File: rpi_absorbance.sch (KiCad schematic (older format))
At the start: 33 parts, among them CON1 BARREL_JACK, P1 CONN_02X04, P2 CONN_01X02, P3 RPI_HEADER, P4 STEPPER_CONN, P5 CONN_02X05, Q1 ZTX692B, U1 R-78B5.0-1.5L, U2 MUN5216DW1T1G, U3 DRV8825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

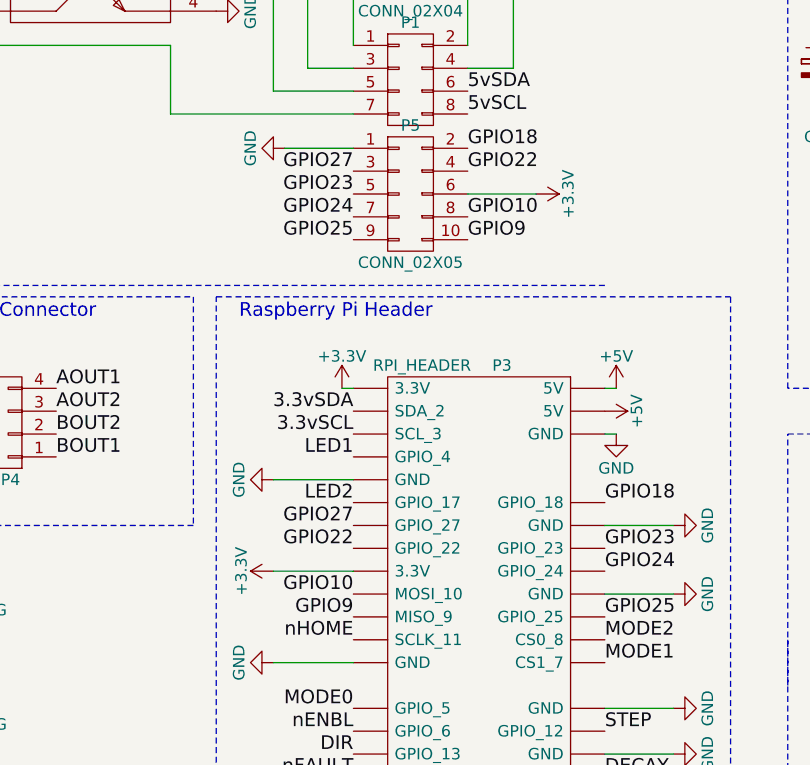
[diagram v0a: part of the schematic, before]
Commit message: Add missing connections
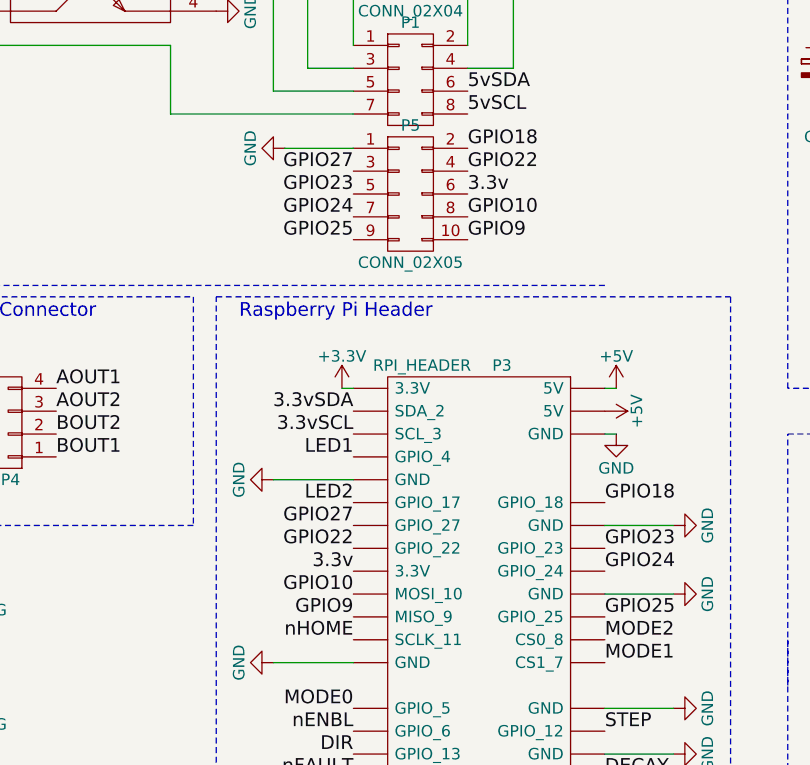
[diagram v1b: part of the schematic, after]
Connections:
- net +3V3: no longer P3.17 (3.3V), P5.6 (P6)
- new net 3.3v: P3.17 (3.3V), P5.6 (P6)
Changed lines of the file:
@@
 LED1
-$Comp
-L +3.3V #PWR021
-U 1 1 56CC6368
-P 2750 6050
-F 0 "#PWR021" H 2750 5900 50  0001 C CNN
-F 1 "+3.3V" H 2750 6190 50  0000 C CNN
-F 2 "" H 2750 6050 50  0000 C CNN
-F 3 "" H 2750 6050 50  0000 C CNN
-	1    2750 6050
-	0    -1   -1   0
-$EndComp
 $Comp
 L PWR_FLAG #FLG022
@@
 Text Notes 5100 2800 0    60   ~ 0
 Stepper Motor Driver
-$Comp
-L +3.3V #PWR040
-U 1 1 56CD7200
-P 3900 4400
-F 0 "#PWR040" H 3900 4250 50  0001 C CNN
-F 1 "+3.3V" H 3900 4540 50  0000 C CNN
-F 2 "" H 3900 4400 50  0000 C CNN
-F 3 "" H 3900 4400 50  0000 C CNN
-	1    3900 4400
-	0    1    1    0
-$EndComp
 $Comp
 L RPI_HEADER P3
@@
 Wire Notes Line
 	5000 5250 5000 2700
-Wire Wire Line
-	2750 6050 3100 6050
 Wire Notes Line
 	2500 4850 4750 4850
@@
 Text Label 3100 4600 2    60   ~ 0
 GPIO25
-Wire Wire Line
-	3900 4400 3600 4400
 Text Label 3100 4300 2    60   ~ 0
 GPIO27
@@
 $EndComp
 Connection ~ 2300 2500
+Text Label 3100 6050 2    60   ~ 0
+3.3v
+Text Label 3600 4400 0    60   ~ 0
+3.3v
 $EndSCHEMATC

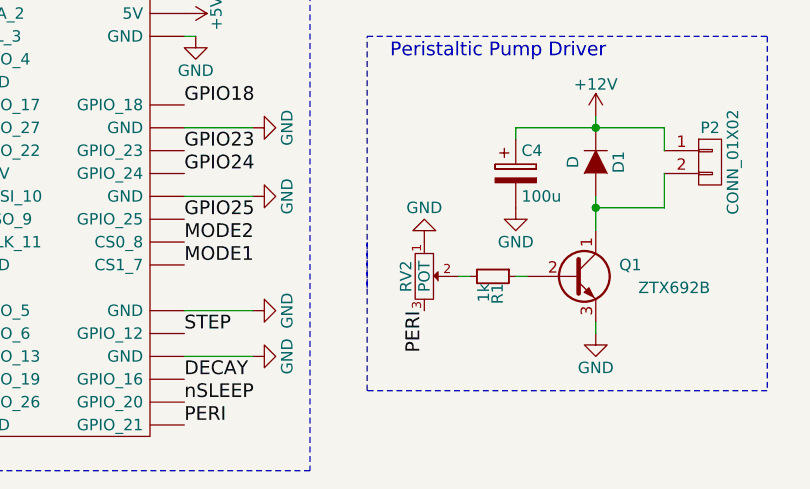
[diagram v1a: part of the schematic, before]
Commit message: Replace power input footprint
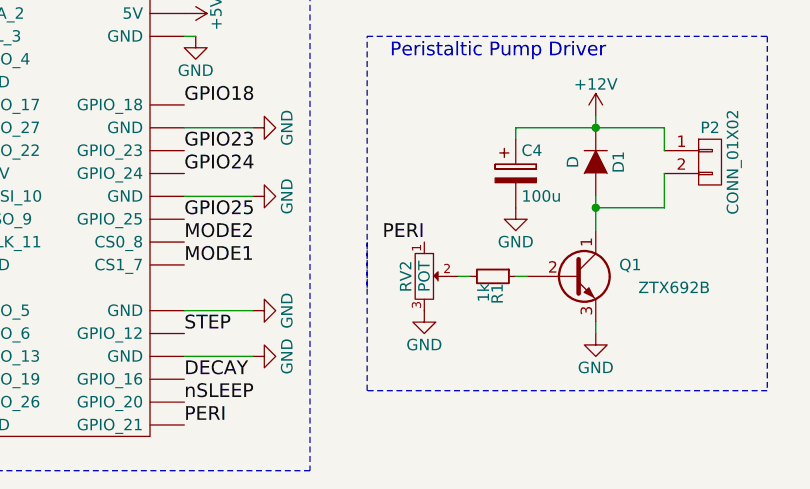
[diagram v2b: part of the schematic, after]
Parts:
- CON1: footprint footprints:CUI_BARREL_JACK -> footprints:CUI_PJ-002AH-SMT
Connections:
- net GND: now also RV2.3; no longer RV2.1
- net PERI: now also RV2.1; no longer RV2.3
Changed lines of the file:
@@
 LED1
 $Comp
-L PWR_FLAG #FLG022
+L PWR_FLAG #FLG021
 U 1 1 56CC8492
 P 900 6400
-F 0 "#FLG022" H 900 6495 50  0001 C CNN
+F 0 "#FLG021" H 900 6495 50  0001 C CNN
 F 1 "PWR_FLAG" H 900 6580 50  0000 C CNN
 F 2 "" H 900 6400 50  0000 C CNN
@@
 $EndComp
 $Comp
-L +5V #PWR023
+L +5V #PWR022
 U 1 1 56CC84E3
 P 900 6450
-F 0 "#PWR023" H 900 6300 50  0001 C CNN
+F 0 "#PWR022" H 900 6300 50  0001 C CNN
 F 1 "+5V" H 900 6590 50  0000 C CNN
 F 2 "" H 900 6450 50  0000 C CNN
@@
 $EndComp
 $Comp
-L +12V #PWR024
+L +12V #PWR023
 U 1 1 56CC852D
 P 1400 6450
-F 0 "#PWR024" H 1400 6300 50  0001 C CNN
+F 0 "#PWR023" H 1400 6300 50  0001 C CNN
 F 1 "+12V" H 1400 6590 50  0000 C CNN
 F 2 "" H 1400 6450 50  0000 C CNN
@@
 $EndComp
 $Comp
-L GND #PWR025
+L GND #PWR024
 U 1 1 56CC8577
 P 900 6950
-F 0 "#PWR025" H 900 6700 50  0001 C CNN
+F 0 "#PWR024" H 900 6700 50  0001 C CNN
 F 1 "GND" H 900 6800 50  0000 C CNN
 F 2 "" H 900 6950 50  0000 C CNN
@@
 $EndComp
 $Comp
-L +3.3V #PWR026
+L +3.3V #PWR025
 U 1 1 56CC85C1
 P 1400 6950
-F 0 "#PWR026" H 1400 6800 50  0001 C CNN
+F 0 "#PWR025" H 1400 6800 50  0001 C CNN
 F 1 "+3.3V" H 1400 7090 50  0000 C CNN
 F 2 "" H 1400 6950 50  0000 C CNN
@@
 $EndComp
 $Comp
-L PWR_FLAG #FLG027
+L PWR_FLAG #FLG026
 U 1 1 56CC860B
 P 1400 6400
-F 0 "#FLG027" H 1400 6495 50  0001 C CNN
+F 0 "#FLG026" H 1400 6495 50  0001 C CNN
 F 1 "PWR_FLAG" H 1400 6580 50  0000 C CNN
 F 2 "" H 1400 6400 50  0000 C CNN
@@
 $EndComp
 $Comp
-L PWR_FLAG #FLG028
+L PWR_FLAG #FLG027
 U 1 1 56CC8655
 P 900 6900
-F 0 "#FLG028" H 900 6995 50  0001 C CNN
+F 0 "#FLG027" H 900 6995 50  0001 C CNN
 F 1 "PWR_FLAG" H 900 7080 50  0000 C CNN
 F 2 "" H 900 6900 50  0000 C CNN
@@
 $EndComp
 $Comp
-L PWR_FLAG #FLG029
+L PWR_FLAG #FLG028
 U 1 1 56CC88FF
 P 1400 6900
-F 0 "#FLG029" H 1400 6995 50  0001 C CNN
+F 0 "#FLG028" H 1400 6995 50  0001 C CNN
 F 1 "PWR_FLAG" H 1400 7080 50  0000 C CNN
 F 2 "" H 1400 6900 50  0000 C CNN
@@
 $EndComp
 $Comp
-L GND #PWR030
+L GND #PWR029
 U 1 1 56CCD79A
 P 5500 3350
-F 0 "#PWR030" H 5500 3100 50  0001 C CNN
+F 0 "#PWR029" H 5500 3100 50  0001 C CNN
 F 1 "GND" H 5500 3200 50  0000 C CNN
 F 2 "" H 5500 3350 50  0000 C CNN
@@
 $EndComp
 $Comp
-L +12V #PWR031
+L +12V #PWR030
 U 1 1 56CCD97B
 P 5150 3600
-F 0 "#PWR031" H 5150 3450 50  0001 C CNN
+F 0 "#PWR030" H 5150 3450 50  0001 C CNN
 F 1 "+12V" H 5150 3740 50  0000 C CNN
 F 2 "" H 5150 3600 50  0000 C CNN
@@
 $EndComp
 $Comp
-L GND #PWR032
+L GND #PWR031
 U 1 1 56CCDA4E
 P 5150 4000
-F 0 "#PWR032" H 5150 3750 50  0001 C CNN
+F 0 "#PWR031" H 5150 3750 50  0001 C CNN
 F 1 "GND" H 5150 3850 50  0000 C CNN
 F 2 "" H 5150 4000 50  0000 C CNN
@@
 $EndComp
 $Comp
-L GND #PWR033
+L GND #PWR032
 U 1 1 56CCE1B7
 P 5500 4650
-F 0 "#PWR033" H 5500 4400 50  0001 C CNN
+F 0 "#PWR032" H 5500 4400 50  0001 C CNN
 F 1 "GND" H 5500 4500 50  0000 C CNN
 F 2 "" H 5500 4650 50  0000 C CNN
@@
 BOUT1
 $Comp
-L GND #PWR034
+L GND #PWR033
 U 1 1 56CCE5FE
 P 5550 4000
-F 0 "#PWR034" H 5550 3750 50  0001 C CNN
+F 0 "#PWR033" H 5550 3750 50  0001 C CNN
 F 1 "GND" H 5550 3850 50  0000 C CNN
 F 2 "" H 5550 4000 50  0000 C CNN
@@
 $EndComp
 $Comp
-L GND #PWR035
+L GND #PWR034
 U 1 1 56CCF77F
 P 6150 4700
-F 0 "#PWR035" H 6150 4450 50  0001 C CNN
+F 0 "#PWR034" H 6150 4450 50  0001 C CNN
 F 1 "GND" H 6150 4550 50  0000 C CNN
 F 2 "" H 6150 4700 50  0000 C CNN
@@
 $EndComp
 $Comp
-L GND #PWR036
+L GND #PWR035
 U 1 1 56CCF8BA
 P 7350 3300
-F 0 "#PWR036" H 7350 3050 50  0001 C CNN
+F 0 "#PWR035" H 7350 3050 50  0001 C CNN
 F 1 "GND" H 7350 3150 50  0000 C CNN
 F 2 "" H 7350 3300 50  0000 C CNN
@@
 $EndComp
 $Comp
-L GND #PWR037
+L GND #PWR036
 U 1 1 56CCFB5A
 P 6700 4950
-F 0 "#PWR037" H 6700 4700 50  0001 C CNN
+F 0 "#PWR036" H 6700 4700 50  0001 C CNN
 F 1 "GND" H 6700 4800 50  0000 C CNN
 F 2 "" H 6700 4950 50  0000 C CNN
@@
 $EndComp
 $Comp
-L GND #PWR038
+L GND #PWR037
 U 1 1 56CD0763
 P 5850 4550
-F 0 "#PWR038" H 5850 4300 50  0001 C CNN
+F 0 "#PWR037" H 5850 4300 50  0001 C CNN
 F 1 "GND" H 5850 4400 50  0000 C CNN
 F 2 "" H 5850 4550 50  0000 C CNN
@@
 $EndComp
 $Comp
-L GND #PWR039
+L GND #PWR038
 U 1 1 56CD1F0D
 P 7350 4950
-F 0 "#PWR039" H 7350 4700 50  0001 C CNN
+F 0 "#PWR038" H 7350 4700 50  0001 C CNN
 F 1 "GND" H 7350 4800 50  0000 C CNN
 F 2 "" H 7350 4950 50  0000 C CNN
@@
 F 0 "CON1" H 1500 2450 50  0000 C CNN
 F 1 "BARREL_JACK" H 1400 2000 50  0000 C CNN
-F 2 "footprints:CUI_BARREL_JACK" H 1500 2200 50  0001 C CNN
+F 2 "footprints:CUI_PJ-002AH-SMT" H 1500 2200 50  0001 C CNN
 F 3 "" H 1500 2200 50  0000 C CNN
 	1    1500 2200
@@
 	0    1    1    0
 $EndComp
-Text Label 5250 6650 3    60   ~ 0
+Text Label 5250 6350 2    60   ~ 0
 PERI
 $Comp
-L GND #PWR041
+L GND #PWR039
 U 1 1 56D00D89
 P 5650 6200
-F 0 "#PWR041" H 5650 5950 50  0001 C CNN
+F 0 "#PWR039" H 5650 5950 50  0001 C CNN
 F 1 "GND" H 5650 6050 50  0000 C CNN
 F 2 "" H 5650 6200 50  0000 C CNN
@@
 $EndComp
 $Comp
-L +12V #PWR042
+L +12V #PWR040
 U 1 1 56D01707
 P 6000 5800
-F 0 "#PWR042" H 6000 5650 50  0001 C CNN
+F 0 "#PWR040" H 6000 5650 50  0001 C CNN
 F 1 "+12V" H 6000 5940 50  0000 C CNN
 F 2 "" H 6000 5800 50  0000 C CNN
@@
 $EndComp
 $Comp
-L GND #PWR043
+L GND #PWR041
 U 1 1 56D018B9
 P 6000 6750
-F 0 "#PWR043" H 6000 6500 50  0001 C CNN
+F 0 "#PWR041" H 6000 6500 50  0001 C CNN
 F 1 "GND" H 6000 6600 50  0000 C CNN
 F 2 "" H 6000 6750 50  0000 C CNN
@@
 PERI
 $Comp
-L +12V #PWR044
+L +12V #PWR042
 U 1 1 56D24636
 P 2900 3500
-F 0 "#PWR044" H 2900 3350 50  0001 C CNN
+F 0 "#PWR042" H 2900 3350 50  0001 C CNN
 F 1 "+12V" H 2900 3640 50  0000 C CNN
 F 2 "" H 2900 3500 50  0000 C CNN
@@
 $EndComp
 $Comp
-L GND #PWR045
+L GND #PWR043
 U 1 1 56D248DC
 P 3600 3500
-F 0 "#PWR045" H 3600 3250 50  0001 C CNN
+F 0 "#PWR043" H 3600 3250 50  0001 C CNN
 F 1 "GND" H 3600 3350 50  0000 C CNN
 F 2 "" H 3600 3500 50  0000 C CNN
@@
 $EndComp
 $Comp
-L GND #PWR046
+L GND #PWR044
 U 1 1 56D251E1
 P 3100 3500
-F 0 "#PWR046" H 3100 3250 50  0001 C CNN
+F 0 "#PWR044" H 3100 3250 50  0001 C CNN
 F 1 "GND" H 3100 3350 50  0000 C CNN
 F 2 "" H 3100 3500 50  0000 C CNN
@@
 LED2
 $Comp
-L GND #PWR047
+L GND #PWR045
 U 1 1 56D2C382
 P 2800 4200
-F 0 "#PWR047" H 2800 3950 50  0001 C CNN
+F 0 "#PWR045" H 2800 3950 50  0001 C CNN
 F 1 "GND" H 2800 4050 50  0000 C CNN
 F 2 "" H 2800 4200 50  0000 C CNN
@@
 $EndComp
 $Comp
-L GND #PWR048
+L GND #PWR046
 U 1 1 56D3407A
 P 1400 3250
-F 0 "#PWR048" H 1400 3000 50  0001 C CNN
+F 0 "#PWR046" H 1400 3000 50  0001 C CNN
 F 1 "GND" H 1400 3100 50  0000 C CNN
 F 2 "" H 1400 3250 50  0000 C CNN
@@
 $EndComp
 $Comp
-L GND #PWR049
+L GND #PWR047
 U 1 1 56D340E8
 P 2500 3600
-F 0 "#PWR049" H 2500 3350 50  0001 C CNN
+F 0 "#PWR047" H 2500 3350 50  0001 C CNN
 F 1 "GND" H 2500 3450 50  0000 C CNN
 F 2 "" H 2500 3600 50  0000 C CNN
@@
 $EndComp
 $Comp
-L GND #PWR050
+L GND #PWR048
 U 1 1 56D3711B
-P 5250 6350
-F 0 "#PWR050" H 5250 6100 50  0001 C CNN
-F 1 "GND" H 5250 6200 50  0000 C CNN
-F 2 "" H 5250 6350 50  0000 C CNN
-F 3 "" H 5250 6350 50  0000 C CNN
-	1    5250 6350
-	-1   0    0    1
+P 5250 6650
+F 0 "#PWR048" H 5250 6400 50  0001 C CNN
+F 1 "GND" H 5250 6500 50  0000 C CNN
+F 2 "" H 5250 6650 50  0000 C CNN
+F 3 "" H 5250 6650 50  0000 C CNN
+	1    5250 6650
+	1    0    0    -1
 $EndComp
 Text Notes 1200 2800 0    60   ~ 0

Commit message: Reorganize pcb
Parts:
- removed P5: CONN_02X05, Pin_Headers:Pin_Header_Straight_2x05, symbol CONN_02X05
- removed U2: MUN5216DW1T1G, footprints:SOT−363, symbol MUN5216DW1T1G
- added P5: CONN_02X06, Pin_Headers:Pin_Header_Straight_2x06, symbol CONN_02X06
- added U2: NXP_PUMH10, footprints:SOT−363, symbol 2xNPN_R1_R2
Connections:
- net +5V: now also P5.11 (P11)
- net 3.3v: now also P5.6 (P6)
- net GND: now also P5.1 (P1), P5.12 (P12), U2.1, U2.4
- net GPIO10: now also P5.8 (P8)
- net GPIO18: now also P5.2 (P2)
- net GPIO22: now also P5.4 (P4)
- net GPIO23: now also P5.5 (P5)
- net GPIO24: now also P5.7 (P7)
- net GPIO25: now also P5.9 (P9)
- net GPIO27: now also P5.3 (P3)
- net GPIO9: now also P5.10 (P10)
- net at P1.7 (P7): now also U2.3
- net at P1.5 (P5): now also U2.6
- net LED1 renamed PDN1
- net PDN1: now also U2.2
- net LED2 renamed PDN2
- net PDN2: now also U2.5
- net PERI renamed PDN3
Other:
- moved on the sheet: P1
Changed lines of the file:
@@
 L +5V #PWR03
 U 1 1 56CB8BD2
-P 3800 3500
-F 0 "#PWR03" H 3800 3350 50  0001 C CNN
-F 1 "+5V" H 3800 3640 50  0000 C CNN
-F 2 "" H 3800 3500 50  0000 C CNN
-F 3 "" H 3800 3500 50  0000 C CNN
-	1    3800 3500
-	1    0    0    -1
-$EndComp
-Text Label 3600 3950 0    60   ~ 0
+P 3800 3100
+F 0 "#PWR03" H 3800 2950 50  0001 C CNN
+F 1 "+5V" H 3800 3240 50  0000 C CNN
+F 2 "" H 3800 3100 50  0000 C CNN
+F 3 "" H 3800 3100 50  0000 C CNN
+	1    3800 3100
+	1    0    0    -1
+$EndComp
+Text Label 3600 3550 0    60   ~ 0
 5vSDA
-Text Label 3600 4050 0    60   ~ 0
+Text Label 3600 3650 0    60   ~ 0
 5vSCL
 $Comp
@@
 $EndComp
 Text Label 3100 5550 2    60   ~ 0
-LED1
+PDN1
 $Comp
 L PWR_FLAG #FLG021
@@
 $EndComp
 Text Label 5250 6350 2    60   ~ 0
-PERI
+PDN3
 $Comp
 L GND #PWR039
@@
 $EndComp
 Text Label 4200 7150 0    60   ~ 0
-PERI
+PDN3
 $Comp
 L +12V #PWR042
 U 1 1 56D24636
-P 2900 3500
-F 0 "#PWR042" H 2900 3350 50  0001 C CNN
-F 1 "+12V" H 2900 3640 50  0000 C CNN
-F 2 "" H 2900 3500 50  0000 C CNN
-F 3 "" H 2900 3500 50  0000 C CNN
-	1    2900 3500
+P 2900 3100
+F 0 "#PWR042" H 2900 2950 50  0001 C CNN
+F 1 "+12V" H 2900 3240 50  0000 C CNN
+F 2 "" H 2900 3100 50  0000 C CNN
+F 3 "" H 2900 3100 50  0000 C CNN
+	1    2900 3100
 	1    0    0    -1
 $EndComp
@@
 L GND #PWR043
 U 1 1 56D248DC
-P 3600 3500
-F 0 "#PWR043" H 3600 3250 50  0001 C CNN
-F 1 "GND" H 3600 3350 50  0000 C CNN
-F 2 "" H 3600 3500 50  0000 C CNN
-F 3 "" H 3600 3500 50  0000 C CNN
-	1    3600 3500
+P 3600 3100
+F 0 "#PWR043" H 3600 2850 50  0001 C CNN
+F 1 "GND" H 3600 2950 50  0000 C CNN
+F 2 "" H 3600 3100 50  0000 C CNN
+F 3 "" H 3600 3100 50  0000 C CNN
+	1    3600 3100
 	-1   0    0    1
 $EndComp
@@
 L GND #PWR044
 U 1 1 56D251E1
-P 3100 3500
-F 0 "#PWR044" H 3100 3250 50  0001 C CNN
-F 1 "GND" H 3100 3350 50  0000 C CNN
-F 2 "" H 3100 3500 50  0000 C CNN
-F 3 "" H 3100 3500 50  0000 C CNN
-	1    3100 3500
+P 3100 3100
+F 0 "#PWR044" H 3100 2850 50  0001 C CNN
+F 1 "GND" H 3100 2950 50  0000 C CNN
+F 2 "" H 3100 3100 50  0000 C CNN
+F 3 "" H 3100 3100 50  0000 C CNN
+	1    3100 3100
 	-1   0    0    1
 $EndComp
 Text Label 1400 3400 2    60   ~ 0
-LED1
+PDN1
 Text Label 2500 3450 0    60   ~ 0
-LED2
+PDN2
 $Comp
 L GND #PWR045
 U 1 1 56D2C382
-P 2800 4200
-F 0 "#PWR045" H 2800 3950 50  0001 C CNN
-F 1 "GND" H 2800 4050 50  0000 C CNN
-F 2 "" H 2800 4200 50  0000 C CNN
-F 3 "" H 2800 4200 50  0000 C CNN
-	1    2800 4200
+P 2800 3950
+F 0 "#PWR045" H 2800 3700 50  0001 C CNN
+F 1 "GND" H 2800 3800 50  0000 C CNN
+F 2 "" H 2800 3950 50  0000 C CNN
+F 3 "" H 2800 3950 50  0000 C CNN
+	1    2800 3950
 	0    1    1    0
 $EndComp
 Text Label 3100 5750 2    60   ~ 0
-LED2
+PDN2
 Text Label 3100 6150 2    60   ~ 0
 GPIO10
 Text Label 3100 6250 2    60   ~ 0
 GPIO9
-Text Label 3600 4500 0    60   ~ 0
+Text Label 3600 4250 0    60   ~ 0
 GPIO10
-Text Label 3600 4600 0    60   ~ 0
+Text Label 3600 4350 0    60   ~ 0
 GPIO9
-$Comp
-L MUN5216DW1T1G U2
-U 1 1 56D33F0B
-P 1950 3450
-F 0 "U2" H 1950 3900 60  0000 C CNN
-F 1 "MUN5216DW1T1G" H 1950 3800 60  0000 C CNN
-F 2 "footprints:SOT−363" H 1950 3800 60  0001 C CNN
-F 3 "" H 1950 3800 60  0000 C CNN
-	1    1950 3450
-	1    0    0    -1
-$EndComp
 $Comp
 L GND #PWR046
@@
 L CONN_02X04 P1
 U 1 1 56D4EA2B
-P 3350 3900
-F 0 "P1" H 3350 4150 50  0000 C CNN
-F 1 "CONN_02X04" H 3350 4200 50  0000 C CNN
-F 2 "Pin_Headers:Pin_Header_Straight_2x04" H 3350 2700 50  0001 C CNN
-F 3 "" H 3350 2700 50  0000 C CNN
-	1    3350 3900
+P 3350 3500
+F 0 "P1" H 3350 3750 50  0000 C CNN
+F 1 "CONN_02X04" H 3350 3800 50  0000 C CNN
+F 2 "Pin_Headers:Pin_Header_Straight_2x04" H 3350 2300 50  0001 C CNN
+F 3 "" H 3350 2300 50  0000 C CNN
+	1    3350 3500
 	1    0    0    -1
 $EndComp
@@
 	1400 3750 1400 3600
 Wire Wire Line
-	2300 3750 1400 3750
-Wire Wire Line
-	2300 4050 2300 3750
-Wire Wire Line
-	3100 4050 2300 4050
+	1400 3750 2750 3750
 Wire Wire Line
 	2750 3250 2500 3250
 Wire Wire Line
-	2750 3950 2750 3250
-Wire Wire Line
-	3100 3950 2750 3950
-Wire Wire Line
-	2800 4200 3100 4200
-Wire Wire Line
-	2900 3500 2900 3850
-Wire Wire Line
-	3100 3500 3100 3750
-Wire Wire Line
-	2900 3850 3100 3850
+	2800 3950 3100 3950
+Wire Wire Line
+	2900 3100 2900 3450
+Wire Wire Line
+	3100 3100 3100 3350
+Wire Wire Line
+	2900 3450 3100 3450
 Wire Notes Line
 	3350 1600 1100 1600
@@
 	6000 6750 6000 6700
 Wire Wire Line
-	3600 3500 3600 3750
-Wire Wire Line
-	3800 3500 3800 3850
-Wire Wire Line
-	3800 3850 3600 3850
+	3600 3100 3600 3350
+Wire Wire Line
+	3800 3100 3800 3450
+Wire Wire Line
+	3800 3450 3600 3450
 Wire Wire Line
 	2500 2500 2500 2400
-$Comp
-L CONN_02X05 P5
-U 1 1 56D5EE2B
-P 3350 4400
-F 0 "P5" H 3350 4700 50  0000 C CNN
-F 1 "CONN_02X05" H 3350 4100 50  0000 C CNN
-F 2 "Pin_Headers:Pin_Header_Straight_2x05" H 3350 3200 50  0001 C CNN
-F 3 "" H 3350 3200 50  0000 C CNN
-	1    3350 4400
-	1    0    0    -1
-$EndComp
-Text Label 3600 4200 0    60   ~ 0
+Text Label 3600 3950 0    60   ~ 0
 GPIO18
-Text Label 3100 4400 2    60   ~ 0
+Text Label 3100 4150 2    60   ~ 0
 GPIO23
-Text Label 3100 4500 2    60   ~ 0
+Text Label 3100 4250 2    60   ~ 0
 GPIO24
-Text Label 3100 4600 2    60   ~ 0
+Text Label 3100 4350 2    60   ~ 0
 GPIO25
-Text Label 3100 4300 2    60   ~ 0
+Text Label 3100 4050 2    60   ~ 0
 GPIO27
 Text Label 3100 5950 2    60   ~ 0
@@
 Text Label 3100 5850 2    60   ~ 0
 GPIO27
-Text Label 3600 4300 0    60   ~ 0
+Text Label 3600 4050 0    60   ~ 0
 GPIO22
 Connection ~ 2050 2300
@@
 Text Label 3100 6050 2    60   ~ 0
 3.3v
-Text Label 3600 4400 0    60   ~ 0
+Text Label 3600 4150 0    60   ~ 0
 3.3v
+Wire Wire Line
+	2750 3250 2750 3550
+Wire Wire Line
+	2750 3550 3100 3550
+Wire Wire Line
+	2750 3750 2750 3650
+Wire Wire Line
+	2750 3650 3100 3650
+$Comp
+L CONN_02X06 P5
+U 1 1 56D765EF
+P 3350 4200
+F 0 "P5" H 3350 4550 50  0000 C CNN
+F 1 "CONN_02X06" H 3350 3850 50  0000 C CNN
+F 2 "Pin_Headers:Pin_Header_Straight_2x06" H 3350 3000 50  0001 C CNN
+F 3 "" H 3350 3000 50  0000 C CNN
+	1    3350 4200
+	1    0    0    -1
+$EndComp
+$Comp
+L GND #PWR049
+U 1 1 56D766A4
+P 3900 4450
+F 0 "#PWR049" H 3900 4200 50  0001 C CNN
+F 1 "GND" H 3900 4300 50  0000 C CNN
+F 2 "" H 3900 4450 50  0000 C CNN
+F 3 "" H 3900 4450 50  0000 C CNN
+	1    3900 4450
+	0    -1   -1   0
+$EndComp
+Wire Wire Line
+	3900 4450 3600 4450
+$Comp
+L +5V #PWR050
+U 1 1 56D767E9
+P 2800 4450
+F 0 "#PWR050" H 2800 4300 50  0001 C CNN
+F 1 "+5V" H 2800 4590 50  0000 C CNN
+F 2 "" H 2800 4450 50  0000 C CNN
+F 3 "" H 2800 4450 50  0000 C CNN
+	1    2800 4450
+	0    -1   -1   0
+$EndComp
+Wire Wire Line
+	3100 4450 2800 4450
+$Comp
+L 2xNPN_R1_R2 U2
+U 1 1 56D77B7D
+P 1950 3450
+F 0 "U2" H 1950 3150 60  0000 C CNN
+F 1 "NXP_PUMH10" H 1950 3800 60  0000 C CNN
+F 2 "footprints:SOT−363" H 1950 3800 60  0001 C CNN
+F 3 "" H 1950 3800 60  0000 C CNN
+	1    1950 3450
+	1    0    0    -1
+$EndComp
 $EndSCHEMATC
